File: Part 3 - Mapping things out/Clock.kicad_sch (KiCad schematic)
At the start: 59 parts, among them SW2 MODE, SW3 SPEED, SW4 BOOT SPEED, SW5 BOOT MODE, SW6 TURBO, SW7 STEP, SW8 TURBO, U3 74AHC14, U4 74AHC74, U5 74AHC74, U6 74AHC74, U7 LMC555, U8 74HC251, U9 74AHC74, X1 14.7456MHz

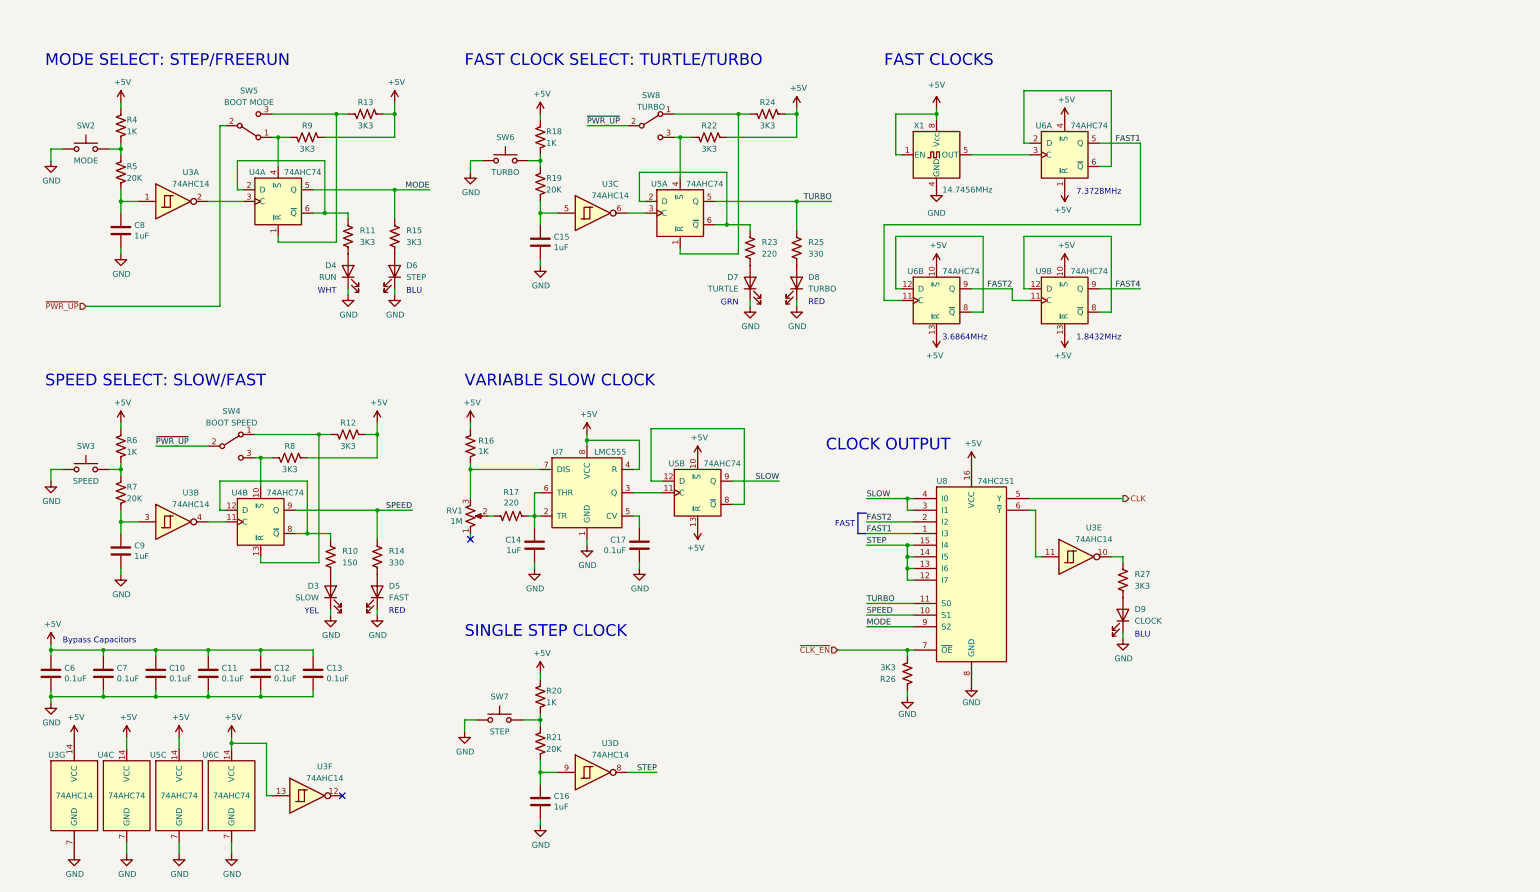
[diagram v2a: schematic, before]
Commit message: Added software selectable speed control
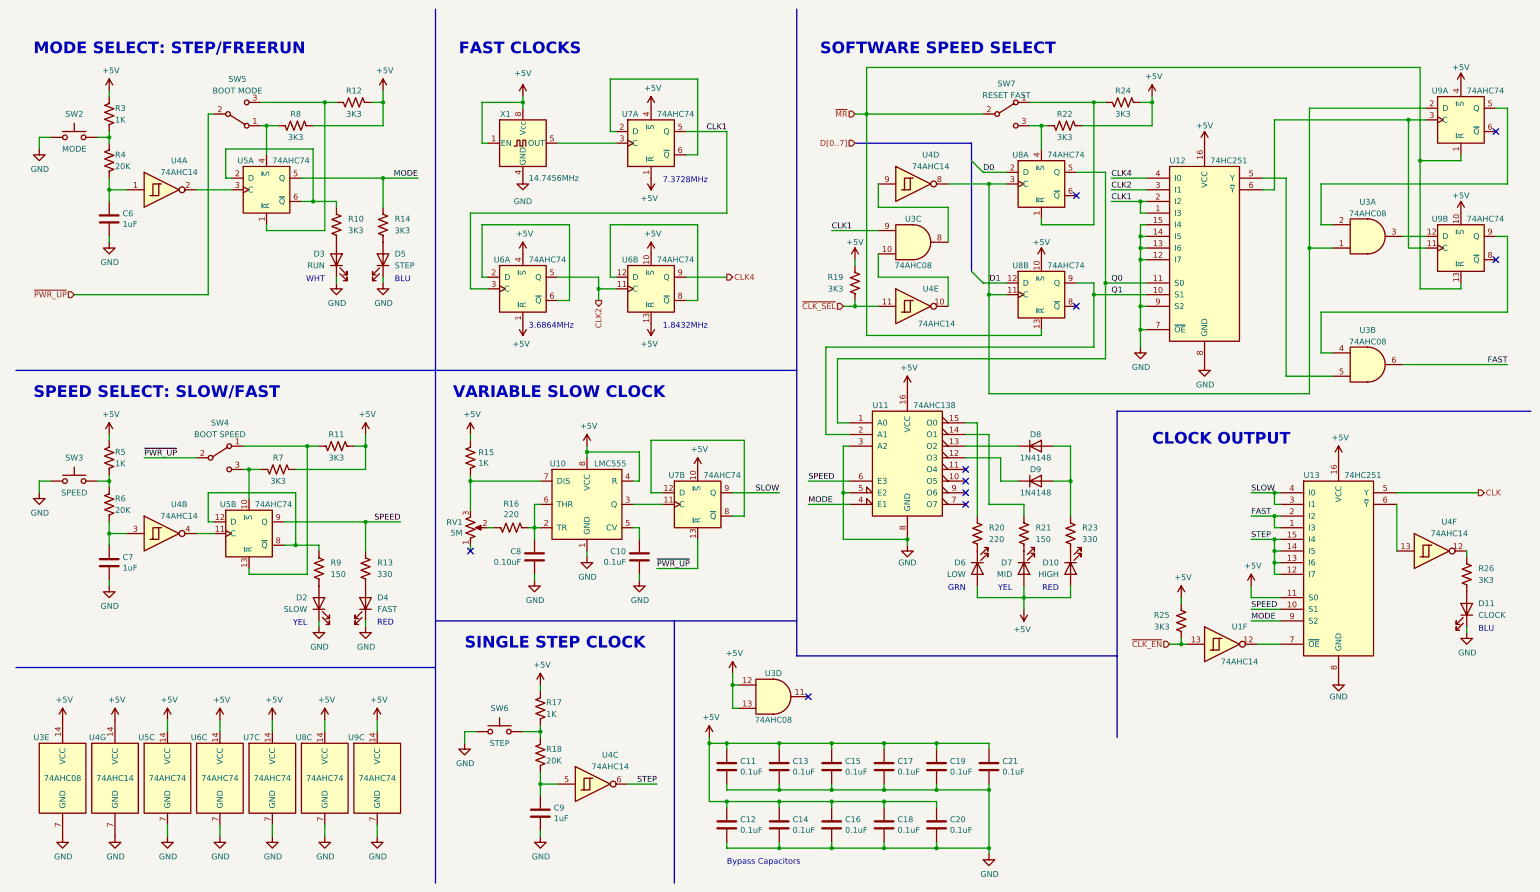
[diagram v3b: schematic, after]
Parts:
- removed C15: 1uF, Capacitor_THT:C_Disc_D3.0mm_W1.6mm_P2.50mm, symbol Device:C
- removed R18: 1K, Resistor_THT:R_Axial_DIN0207_L6.3mm_D2.5mm_P10.16mm_Horizontal, symbol Device:R_US
- removed SW6: TURBO, Button_Switch_THT:SW_PUSH_6mm, symbol Switch:SW_Push
- removed SW8: TURBO, 0_Z80_Library:Microswitch_2.54mm_spacing, symbol Switch:SW_SPDT
- removed unit 3 of U3
- removed unit 1 of U5
- added C12, C14, C16, C18, C20: 0.1uF, Capacitor_THT:C_Disc_D3.0mm_W1.6mm_P2.50mm, symbol Device:C
- added D7: MID, LED_THT:LED_D3.0mm, symbol Device:LED
- added D8, D9: 1N4148, Diode_THT:D_DO-35_SOD27_P7.62mm_Horizontal, symbol Diode:1N4148
- added R21: 150, Resistor_THT:R_Axial_DIN0207_L6.3mm_D2.5mm_P10.16mm_Horizontal, symbol Device:R_US
- added SW7: RESET FAST, 0_Z80_Library:Microswitch_2.54mm_spacing, symbol Switch:SW_SPDT
- added U1: 74AHC14, Package_DIP:DIP-14_W7.62mm_Socket, symbol 74xx:74HC14
- added U11: 74AHC138, Package_DIP:DIP-16_W7.62mm_Socket, symbol 74xx:74LS138
- added U12: 74HC251, Package_DIP:DIP-16_W7.62mm_Socket, symbol 74xx:74LS251
- added U3: 74AHC08, Package_DIP:DIP-14_W7.62mm_Socket, symbol 74xx:74LS08
- added unit 5 of U4
- added U8, U9: 74AHC74, Package_DIP:DIP-14_W7.62mm_Socket, symbol 74xx:74LS74
- C8: renamed from C14; value 1uF -> 0.10uF
- D10: renamed from D8; value TURBO -> HIGH
- D6: renamed from D7; value TURTLE -> LOW
- R19: value 20K -> 3K3
- RV1: value 1M -> 5M; footprint Potentiometer_THT:Potentiometer_Bourns_3299Y_Vertical -> Potentiometer_THT:Potentiometer_Bourns_3006P_Horizontal
- SW2, SW3: footprint Button_Switch_THT:SW_PUSH_6mm -> Button_Switch_THT:SW_Tactile_SPST_Angled_PTS645Vx58-2LFS
- SW6: renamed from SW7; footprint Button_Switch_THT:SW_PUSH_6mm -> Button_Switch_THT:SW_Tactile_SPST_Angled_PTS645Vx58-2LFS
- U10: renamed from U7; footprint Package_DIP:DIP-14_W7.62mm_Socket -> Package_DIP:DIP-8_W7.62mm_Socket
- U13: renamed from U8; footprint Package_DIP:DIP-14_W7.62mm_Socket -> Package_DIP:DIP-16_W7.62mm_Socket
- renumbered C17 to C10, C6 to C11, C7 to C13, C10 to C15, C11 to C17, C12 to C19, C13 to C21, C8 to C6, C9 to C7, C16 to C9, D9 to D11, D3 to D2, D4 to D3, D5 to D4, D6 to D5, R11 to R10, R12 to R11, R13 to R12, R14 to R13, R15 to R14, R16 to R15, R17 to R16, R20 to R17, R21 to R18, R23 to R20, R25 to R23, R26 to R25, R27 to R26, R4 to R3, R5 to R4, R6 to R5, R7 to R6, R8 to R7, R9 to R8, R10 to R9, U3 to U4, U4 to U5, U9 to U6, U5 to U6, U5 to U7, U6 to U7
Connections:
- net +5V: now also D10.2 (A), D6.2 (A), R19.2, R25.2, U13.11 (S0), U6.1 (~{R}), U6.4 (~{S}), C12.1, C14.1, C16.1, C18.1, C20.1, D7.2 (A), U11.16 (VCC), U12.16 (VCC), U3.12, U3.13, U3.14 (VCC), U8.10 (~{S}), U8.14 (VCC), U9.10 (~{S}), U9.14 (VCC), U9.4 (~{S}); no longer U4.13, U6.10 (~{S}), U6.13 (~{R}), U7.13 (~{R})
- net GND: now also C12.2, C14.2, C16.2, C18.2, C20.2, U11.3 (A2), U11.5 (E2), U11.8 (GND), U12.12 (I7), U12.13 (I6), U12.14 (I5), U12.15 (I4), U12.7 (~{OE}), U12.8 (GND), U12.9 (S2), U3.7 (GND), U8.7 (GND), U9.7 (GND); no longer D10.1 (K), D6.1 (K), R25.2
- net MODE: now also U11.4 (E1)
- net SPEED: now also U11.6 (E3)
- net STEP: now also U4.6; no longer U4.8
- net ~{CLK_EN}: now also U1.13; no longer U13.7 (~{OE})
- net ~{PWR_UP}: now also U7.13 (~{R})
- net ~{CLK_SEL}: now reaches R19.1
- net ~{CLK_SEL}: now also U4.11
- net at R23.2: now also D10.1 (K); no longer D10.2 (A)
- net at R22.1: now also SW7.3 (C), U8.4 (~{S})
- net at R24.1: now also SW7.1 (A), U8.1 (~{R})
- net at C9.1, R18.1: now also U4.5; no longer U4.9
- net at U13.6 (~{Y}): now also U4.13; no longer U4.11
- net at R26.1: now also U4.12; no longer U4.10
- net at R20.1: now also U11.15 (O0)
- net at R20.2: now also D6.1 (K); no longer D6.2 (A)
- removed net FAST1: U13.1 (I3), U6.11 (C), U7.5 (Q)
- removed net FAST2: U13.2 (I2), U6.11 (C), U6.9 (Q)
- net FAST4 renamed CLK4
- net CLK4: now also U12.4 (I0)
- net TURBO: no longer names the net of R23.1
- net TURBO: now also D8.2 (A), D9.2 (A); no longer U13.11 (S0)
- new net: U3.10, U4.10
- new net: U3.8, U4.9
- new net: U3.4, U9.9 (Q)
- new net: U12.5 (Y), U3.5
- new net: R21.1, U11.14 (O1)
- new net: D7.1 (K), R21.2
- new net: U12.6 (~{Y}), U9.11 (C), U9.3 (C)
- new net: U3.1, U4.8, U8.11 (C), U8.3 (C), U9.2 (D)
- new net: D9.1 (K), U11.12 (O3)
- new net: U1.12, U13.7 (~{OE})
- new net: D8.1 (K), U11.13 (O2)
- new net: U3.3, U9.12 (D)
- new net: U6.2 (D), U6.6 (~{Q})
- new net: U3.2, U9.5 (Q)
- new net CLK1: U12.1 (I3), U12.2 (I2), U3.9, U6.3 (C), U7.5 (Q)
- new net CLK2: U12.3 (I1), U6.11 (C), U6.5 (Q)
- new net D0: U8.2 (D)
- new net D1: U8.12 (D)
- new net FAST: U13.1 (I3), U13.2 (I2), U3.6
- new net Q0: U11.1 (A0), U12.11 (S0), U8.5 (Q)
- new net Q1: U11.2 (A1), U12.10 (S1), U8.9 (Q)
- new net ~{MR}: SW7.2 (B), U8.13 (~{R}), U9.1 (~{R}), U9.13 (~{R})
- no-connect marks 2 -> 10
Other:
- note added: "SOFTWARE SPEED SELECT"
- note removed: "FAST"
- note removed: "FAST CLOCK SELECT: TURTLE/TURBO"
- company: Frédéric Segard -> Frédéric Segard, aka : Micro Hobbyist
- title: Selectable triple clock circuit -> Manual and software selectable clock
- moved on the sheet: C10, C11, C13, C15, C17, C19, C21, C6, C7, C8, C9, D10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

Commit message: Updated clock, and created CPU card
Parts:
- removed D3: RUN, LED_THT:LED_D3.0mm, symbol Device:LED
- removed D4: FAST, LED_THT:LED_D3.0mm, symbol Device:LED
- removed D8, D9: 1N4148, Diode_THT:D_DO-35_SOD27_P7.62mm_Horizontal, symbol Diode:1N4148
- removed R10, R11, R12, R22, R24, R7, R8: 3K3, Resistor_THT:R_Axial_DIN0207_L6.3mm_D2.5mm_P10.16mm_Horizontal, symbol Device:R_US
- removed R13: 330, Resistor_THT:R_Axial_DIN0207_L6.3mm_D2.5mm_P10.16mm_Horizontal, symbol Device:R_US
- added C20, C21: 0.1uF, Capacitor_THT:C_Disc_D3.0mm_W1.6mm_P2.50mm, symbol Device:C
- added D8: HIGH, LED_THT:LED_D3.0mm_Horizontal_O1.27mm_Z2.0mm_Clear, symbol Device:LED
- added R18: 330, Resistor_THT:R_Axial_DIN0207_L6.3mm_D2.5mm_P10.16mm_Horizontal, symbol Device:R_US
- added RN1: 3K3, Resistor_THT:R_Array_SIP9, symbol Device:R_Network08_US
- added SW8: RESET FAST Q1, 0_Z80_Library:Microswitch_4.7mm_spacing, symbol Switch:SW_SPDT
- added unit 3 of U10
- added unit 2 of U7
- added unit 1 of U7
- C9: renamed from C8; value 0.10uF -> 0.1uF
- D3: renamed from D2; footprint LED_THT:LED_D3.0mm -> LED_THT:LED_D3.0mm_Horizontal_O1.27mm_Z2.0mm_Clear
- D4: renamed from D5; footprint LED_THT:LED_D3.0mm -> LED_THT:LED_D3.0mm_Horizontal_O1.27mm_Z2.0mm_Clear
- D5: renamed from D6; value LOW -> SAFE; footprint LED_THT:LED_D3.0mm -> LED_THT:LED_D3.0mm_Horizontal_O1.27mm_Z2.0mm_Clear
- D6: renamed from D7; value MID -> LOW; footprint LED_THT:LED_D3.0mm -> LED_THT:LED_D3.0mm_Horizontal_O1.27mm_Z2.0mm_Clear
- D7: renamed from D10; value HIGH -> MID; footprint LED_THT:LED_D3.0mm -> LED_THT:LED_D3.0mm_Horizontal_O1.27mm_Z2.0mm_Clear
- D9: renamed from D11; footprint LED_THT:LED_D3.0mm -> LED_THT:LED_D3.0mm_Horizontal_O1.27mm_Z2.0mm_Clear
- R10: renamed from R9; value 150 -> 3K3
- R15: renamed from R23; value 330 -> 3K3
- SW5: renamed from SW4; footprint 0_Z80_Library:Microswitch_2.54mm_spacing -> 0_Z80_Library:Microswitch_4.7mm_spacing
- SW6: renamed from SW5; footprint 0_Z80_Library:Microswitch_2.54mm_spacing -> 0_Z80_Library:Microswitch_4.7mm_spacing
- SW7: value RESET FAST -> RESET FAST Q0; footprint 0_Z80_Library:Microswitch_2.54mm_spacing -> 0_Z80_Library:Microswitch_4.7mm_spacing
- X1: footprint Oscillator:Oscillator_DIP-8 -> 0_Z80_Library:DIP-8-4_W7.62mm_Oscillator_Socket
- renumbered C15 to C10, C17 to C11, C10 to C12, C19 to C13, C21 to C14, C12 to C15, C14 to C16, C16 to C17, C20 to C19, C6 to C4, C7 to C5, C9 to C6, C11 to C7, C13 to C8, R14 to R11, R15 to R12, R16 to R13, R19 to R14, R20 to R16, R21 to R17, R25 to R19, R26 to R20, R3 to R4, R4 to R5, R5 to R6, R6 to R7, R17 to R8, R18 to R9, SW6 to SW4, U7 to U10, U10 to U11, U11 to U12, U12 to U13, U13 to U14
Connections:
- net +5V: now also C20.1, C21.1, D8.2 (A), RN1.1 (common), U10.14 (VCC), U7.1 (~{R}), U7.10 (~{S}), U7.13 (~{R}), U7.4 (~{S}); no longer U8.10 (~{S})
- net CLK1: no longer U13.2 (I2), U3.9
- net CLK2: now also U13.2 (I2); no longer U13.3 (I1)
- net CLK4: now also U13.3 (I1), U7.3 (C); no longer U13.4 (I0)
- net GND: now also C20.2, C21.2, U10.7 (GND)
- net ~{MR}: now also SW8.2 (B); no longer U8.13 (~{R})
- net Yout: now reaches U13.5 (Y), U3.5
- net Yout: now also U3.9
- net at R17.1: now also U12.13 (O2); no longer U12.14 (O1)
- net at R17.2: now also D7.1 (K); no longer D6.1 (K)
- net at R15.1: now also U12.15 (O0)
- net at R15.2: now also D5.1 (K); no longer D7.1 (K)
- net R24: now reaches SW7.1 (A), U8.1 (~{R})
- net R24: now also RN1.7 (R6)
- net R20: now reaches SW7.3 (C), U8.4 (~{S})
- net R20: now also RN1.6 (R5)
- net OSC: now reaches U10.3 (C), X1.5 (OUT)
- net R12: now reaches SW5.1 (A), U5.13 (~{R})
- net R12: now also RN1.5 (R4)
- net R9: now reaches SW5.3 (C), U5.10 (~{S})
- net R9: now also RN1.4 (R3)
- net at U12.12 (O3): now also R18.1
- net ~{CLK}: now reaches U14.6 (~{Y}), U4.13
- net R13: now reaches SW6.3 (C), U5.1 (~{R})
- net R13: now also RN1.2 (R1)
- net R10: now reaches SW6.1 (A), U5.4 (~{S})
- net R10: now also RN1.3 (R2)
- net at R16.1: now also U12.14 (O1); no longer U12.15 (O0)
- net at R16.2: now also D6.1 (K); no longer D5.1 (K)
- net ~{CLK_EN} renamed ~{CLK_DIS}
- new net: U7.11 (C), U7.5 (Q)
- new net: U7.12 (D), U7.8 (~{Q})
- new net: D8.1 (K), R18.2
- new net: U7.2 (D), U7.6 (~{Q})
- new net CLK16: U13.4 (I0), U7.9 (Q)
- new net R21: RN1.9 (R8), SW8.1 (A), U8.13 (~{R})
- new net R25: RN1.8 (R7), SW8.3 (C), U8.10 (~{S})
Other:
- note added: "460.8KHz"
- note added: "BLUE"
- company: Frédéric Segard, aka : Micro Hobbyist -> Frédéric Segard
- moved on the sheet: C10, C11, C12, C13, C14, C15, C16, C17, C18, C19, C4, C5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
